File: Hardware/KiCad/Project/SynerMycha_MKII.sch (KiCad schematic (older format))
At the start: 1 part

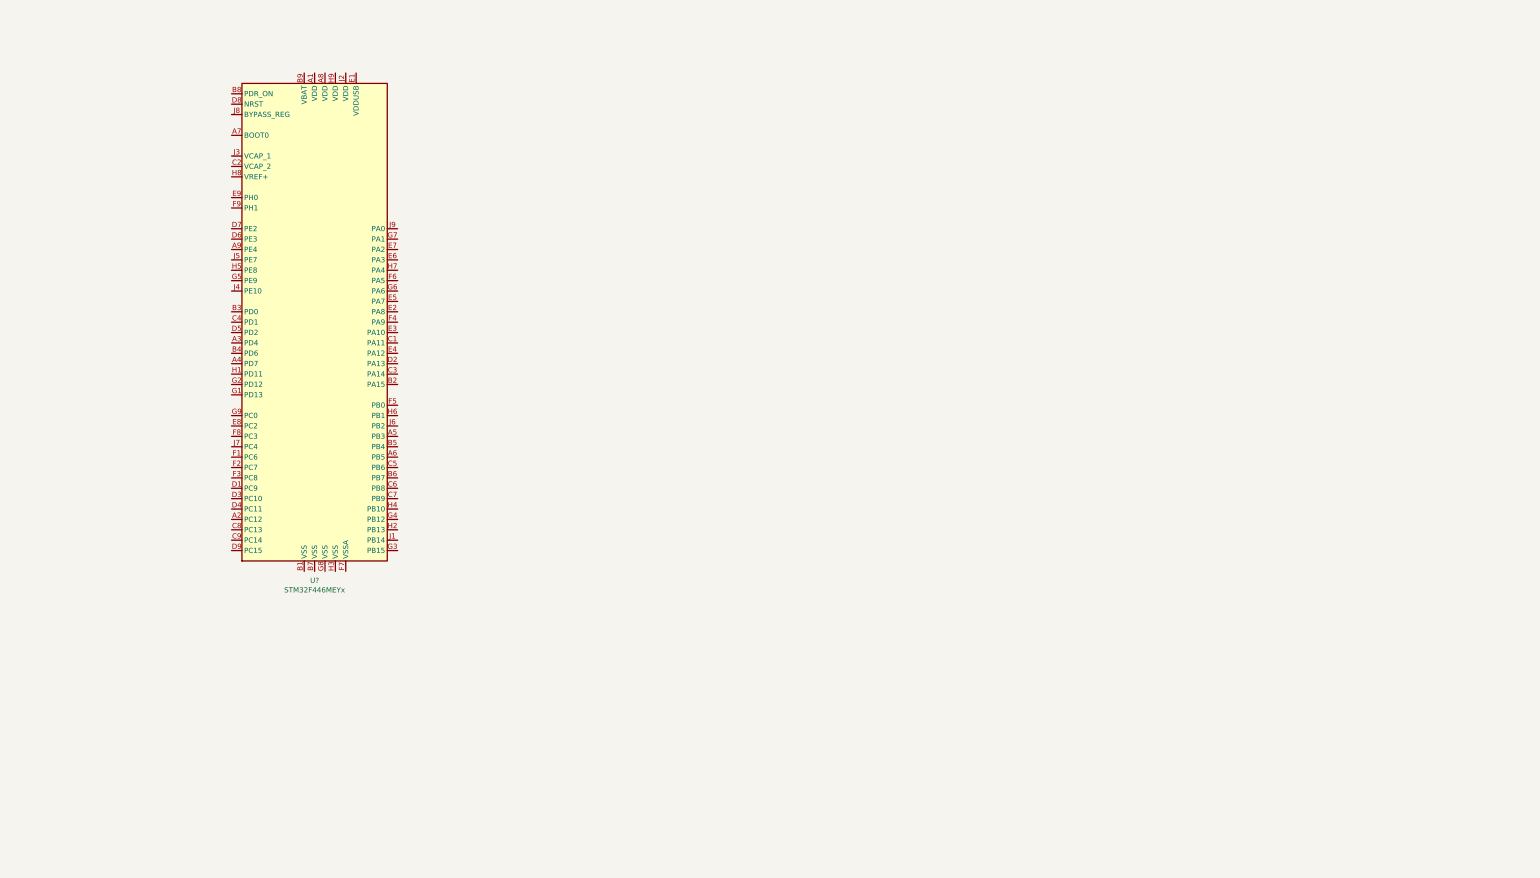
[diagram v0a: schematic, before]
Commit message: Basic uC config, added power and bluetooth antenna
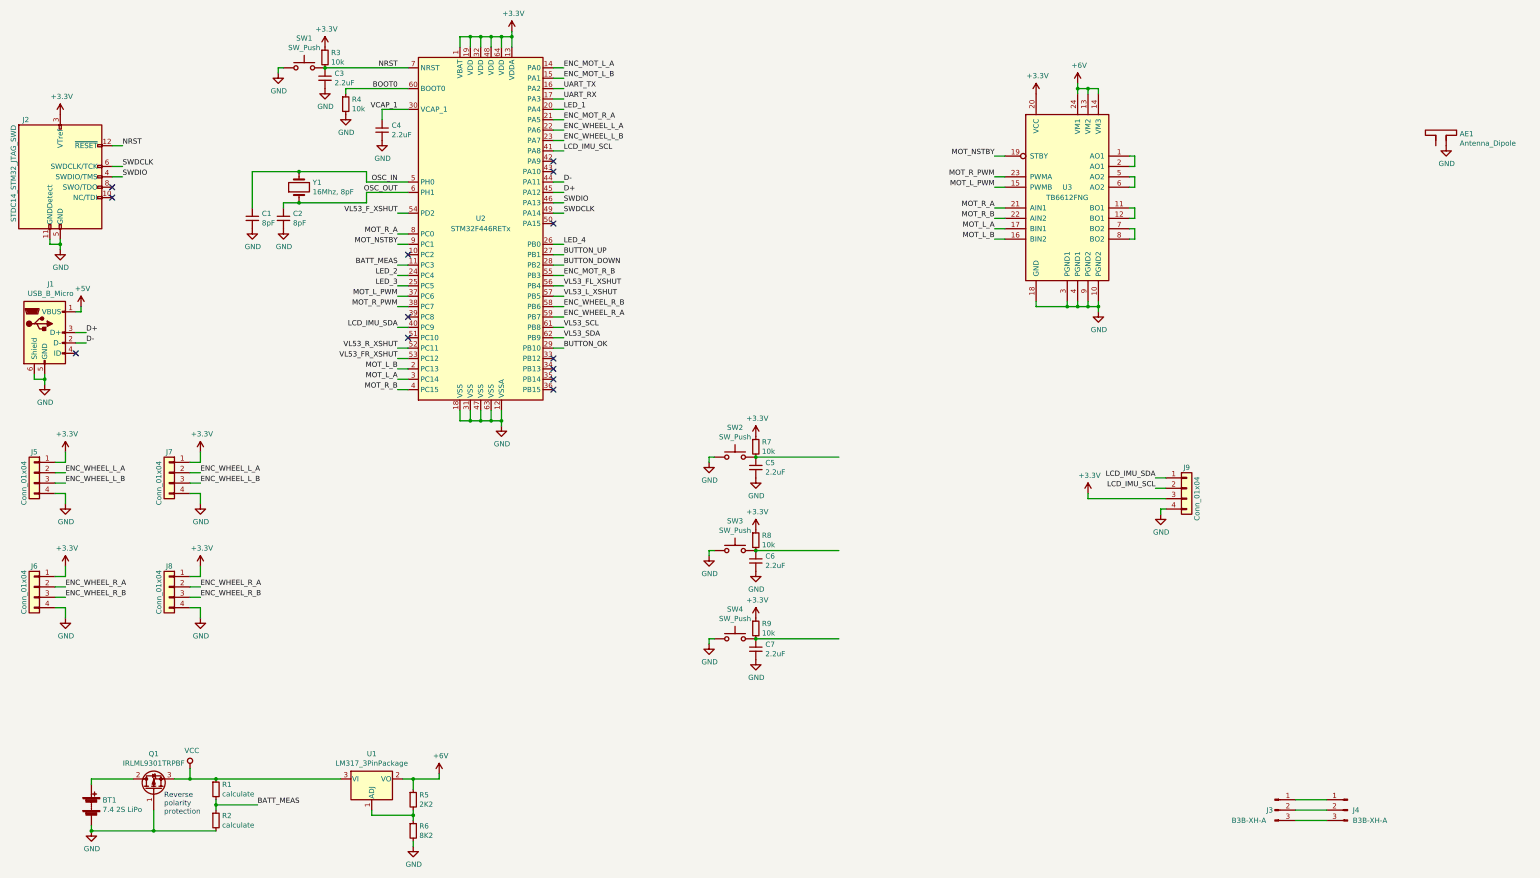
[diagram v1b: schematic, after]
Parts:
- removed U?: STM32F446MEYx, Package_CSP:ST_WLCSP-81_Die421, symbol MCU_ST_STM32F4:STM32F446MEYx
- added AE1: Antenna_Dipole, RF_Antenna:Texas_SWRA117D_2.4GHz_Right, symbol Device:Antenna_Dipole
- added BT1: 7.4 2S LiPo, symbol Device:Battery
- added C1, C2: 8pF, Capacitor_SMD:C_0402_1005Metric, symbol Device:C_Small
- added C3, C4, C5, C6, C7: 2.2uF, Capacitor_SMD:C_0603_1608Metric, symbol Device:C_Small
- added J1: USB_B_Micro, Connector_USB:USB_Micro-B_Amphenol_10103594-0001LF_Horizontal, symbol Connector:USB_B_Micro
- added J2: STDC14_STM32_JTAG_SWD, Connector_PinHeader_1.27mm:PinHeader_2x05_P1.27mm_Vertical_SMD, symbol STM32_STDC14:STDC14_STM32_JTAG_SWD
- added J3, J4: B3B-XH-A, Connector_JST:JST_XH_B3B-XH-A_1x03_P2.50mm_Vertical, symbol Connector:Conn_01x03_Male
- added J5, J6, J7, J8: Conn_01x04, Connector_PinHeader_1.00mm:PinHeader_1x04_P1.00mm_Vertical, symbol Connector_Generic:Conn_01x04
- added J9: Conn_01x04, Connector_PinHeader_2.54mm:PinHeader_1x04_P2.54mm_Vertical, symbol Connector_Generic:Conn_01x04
- added Q1: IRLML9301TRPBF, Package_TO_SOT_SMD:SOT-23, symbol Device:Q_PMOS_GDS
- added R1, R2: calculate, Resistor_SMD:R_0402_1005Metric, symbol Device:R_Small
- added R3, R4, R7, R8, R9: 10k, Resistor_SMD:R_0402_1005Metric, symbol Device:R_Small
- added R5: 2K2, Resistor_SMD:R_0402_1005Metric, symbol Device:R_Small
- added R6: 8K2, Resistor_SMD:R_0402_1005Metric, symbol Device:R_Small
- added SW1, SW2, SW3, SW4: SW_Push, Button_Switch_SMD:SW_SPST_B3U-1000P, symbol Switch:SW_Push
- added U1: LM317_3PinPackage, Package_TO_SOT_SMD:SOT-223, symbol Regulator_Linear:LM317_3PinPackage
- added U2: STM32F446RETx, Package_QFP:LQFP-64_10x10mm_P0.5mm, symbol MCU_ST_STM32F4:STM32F446RETx
- added U3: TB6612FNG, Package_SO:SSOP-24_5.3x8.2mm_P0.65mm, symbol Driver_Motor:TB6612FNG
- added Y1: 16Mhz, 8pF, Crystal:Crystal_SMD_TXC_7A-2Pin_5x3.2mm, symbol Device:Crystal
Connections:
- new net: BT1.1 (+), Q1.2 (D)
- new net: J3.1 (Pin_1), J4.1 (Pin_1)
- new net: J3.2 (Pin_2), J4.2 (Pin_2)
- new net: J3.3 (Pin_3), J4.3 (Pin_3)
- new net: C5.1, R7.2, SW2.2
- new net: C6.1, R8.2, SW3.2
- new net: C7.1, R9.2, SW4.2
- new net: U3.1 (AO1), U3.2 (AO1)
- new net: U3.11 (BO1), U3.12 (BO1)
- new net: U3.5 (AO2), U3.6 (AO2)
- new net: U3.7 (BO2), U3.8 (BO2)
- new net: R5.2, R6.1, U1.1 (ADJ)
- new net +3V3: J2.3 (VTref), J5.1 (Pin_1), J6.1 (Pin_1), J7.1 (Pin_1), J8.1 (Pin_1), J9.3 (Pin_3), R3.1, R7.1, R8.1, R9.1, U2.1 (VBAT), U2.13 (VDDA), U2.19 (VDD), U2.32 (VDD), U2.48 (VDD), U2.64 (VDD), U3.20 (VCC)
- new net +5V: J1.1 (VBUS)
- new net +6V: R5.1, U1.2 (VO), U3.13 (VM2), U3.14 (VM3), U3.24 (VM1)
- new net BATT_MEAS: R1.2, R2.1, U2.11 (PC3)
- new net BOOT0: R4.1, U2.60 (BOOT0)
- new net BUTTON_DOWN: U2.28 (PB2)
- new net BUTTON_OK: U2.29 (PB10)
- new net BUTTON_UP: U2.27 (PB1)
- new net D+: J1.3 (D+), U2.45 (PA12)
- new net D-: J1.2 (D-), U2.44 (PA11)
- new net ENC_MOT_L_A: U2.14 (PA0)
- new net ENC_MOT_L_B: U2.15 (PA1)
- new net ENC_MOT_R_A: U2.21 (PA5)
- new net ENC_MOT_R_B: U2.55 (PB3)
- new net ENC_WHEEL_L_A: J5.2 (Pin_2), J7.2 (Pin_2), U2.22 (PA6)
- new net ENC_WHEEL_L_B: J5.3 (Pin_3), J7.3 (Pin_3), U2.23 (PA7)
- new net ENC_WHEEL_R_A: J6.2 (Pin_2), J8.2 (Pin_2), U2.59 (PB7)
- new net ENC_WHEEL_R_B: J6.3 (Pin_3), J8.3 (Pin_3), U2.58 (PB6)
- new net GND: AE1.2, BT1.2 (-), C1.2, C2.2, C3.2, C4.2, C5.2, C6.2, C7.2, J1.5 (GND), J1.6 (Shield), J2.11 (GNDDetect), J2.5 (GND), J5.4 (Pin_4), J6.4 (Pin_4), J7.4 (Pin_4), J8.4 (Pin_4), J9.4 (Pin_4), Q1.1 (G), R2.2, R4.2, R6.2, SW1.1, SW2.1, SW3.1, SW4.1, U2.12 (VSSA), U2.18 (VSS), U2.31 (VSS), U2.47 (VSS), U2.63 (VSS), U3.10 (PGND2), U3.18 (GND), U3.3 (PGND1), U3.4 (PGND1), U3.9 (PGND2)
- new net LCD_IMU_SCL: J9.2 (Pin_2), U2.41 (PA8)
- new net LCD_IMU_SDA: J9.1 (Pin_1), U2.40 (PC9)
- new net LED_1: U2.20 (PA4)
- new net LED_2: U2.24 (PC4)
- new net LED_3: U2.25 (PC5)
- new net LED_4: U2.26 (PB0)
- new net MOT_L_A: U2.3 (PC14), U3.17 (BIN1)
- new net MOT_L_B: U2.2 (PC13), U3.16 (BIN2)
- new net MOT_L_PWM: U2.37 (PC6), U3.15 (PWMB)
- new net MOT_NSTBY: U2.9 (PC1), U3.19 (STBY)
- new net MOT_R_A: U2.8 (PC0), U3.21 (AIN1)
- new net MOT_R_B: U2.4 (PC15), U3.22 (AIN2)
- new net MOT_R_PWM: U2.38 (PC7), U3.23 (PWMA)
- new net NRST: C3.1, J2.12 (~RESET~), R3.2, SW1.2, U2.7 (NRST)
- new net OSC_IN: C1.1, U2.5 (PH0), Y1.2
- new net OSC_OUT: C2.1, U2.6 (PH1), Y1.1
- new net SWDCLK: J2.6 (SWDCLK/TCK), U2.49 (PA14)
- new net SWDIO: J2.4 (SWDIO/TMS), U2.46 (PA13)
- new net UART_RX: U2.17 (PA3)
- new net UART_TX: U2.16 (PA2)
- new net VCAP_1: C4.1, U2.30 (VCAP_1)
- new net VCC: Q1.3 (S), R1.1, U1.3 (VI)
- new net VL53_FL_XSHUT: U2.56 (PB4)
- new net VL53_FR_XSHUT: U2.53 (PC12)
- new net VL53_F_XSHUT: U2.54 (PD2)
- new net VL53_L_XSHUT: U2.57 (PB5)
- new net VL53_R_XSHUT: U2.52 (PC11)
- new net VL53_SCL: U2.61 (PB8)
- new net VL53_SDA: U2.62 (PB9)
- no-connect marks 0 -> 13
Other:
- note added: "Reverse \npolarity \nprotection"

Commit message: QS
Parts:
- removed AE1: Antenna_Dipole, RF_Antenna:Texas_SWRA117D_2.4GHz_Right, symbol Device:Antenna_Dipole
- removed U3: TB6612FNG, Package_SO:SSOP-24_5.3x8.2mm_P0.65mm, symbol Driver_Motor:TB6612FNG
- added BZ?: Buzzer, symbol Device:Buzzer
- added C10, C12, C13, C8: 0.1uF, Capacitor_SMD:C_0402_1005Metric, symbol Device:C_Small
- added C11, C14, C16, C9: 10uF, Capacitor_SMD:C_0603_1608Metric, symbol Device:C_Small
- added C15: 0.1uF, Capacitor_SMD:C_0603_1608Metric, symbol Device:C_Small
- added J10: USB_B_Micro, Connector_USB:USB_Micro-B_Amphenol_10103594-0001LF_Horizontal, symbol Connector:USB_B_Micro
- added J11: Conn_02x04_Odd_Even, Connector_PinSocket_2.54mm:PinSocket_2x04_P2.54mm_Horizontal, symbol Connector_Generic:Conn_02x04_Odd_Even
- added Q2, Q3: S8050, Package_TO_SOT_THT:TO-92_Inline, symbol Transistor_BJT:S8050
- added R10, R11: 10k, Resistor_SMD:R_0402_1005Metric, symbol Device:R_Small
- added R12, R13: 12k, Resistor_SMD:R_0402_1005Metric, symbol Device:R_Small
- added U3: VL53L0X, VL53L0X:SENSOR_VL53L0X, symbol VL53L0X:VL53L0X
- added U4: DRV8835, Package_SON:Texas_R-PWSON-N12_EP0.4x2mm, symbol KiCad_bibelem:DRV8835
- added U5, U6: AS5045B, Package_SO:SSOP-16_5.3x6.2mm_P0.65mm, symbol Sensor_Magnetic:AS5045B
- added U7: CP2102N-A01-GQFN28, Package_DFN_QFN:QFN-28-1EP_5x5mm_P0.5mm_EP3.35x3.35mm, symbol Interface_USB:CP2102N-A01-GQFN28
- J5, J6: footprint Connector_PinHeader_1.00mm:PinHeader_1x04_P1.00mm_Vertical -> Connector_PinHeader_1.00mm:PinHeader_1x04_P1.00mm_Horizontal
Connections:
- net labels added: ESP_D+, ESP_D-, ESP_VBUS, MOT_L_EN, MOT_L_PH, MOT_R_EN, MOT_R_PH, STM_D+, STM_D-
- net labels removed: D+, D-
- wire segments 191 -> 234
- no-connect marks 13 -> 44
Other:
- note added: "ENCODER BOARDS"
- note added: "MOTOR DRIVER"
- note added: "UI"
- note added: "WiFi"
- moved on the sheet: BT1, C1, C2, C5, C6, C7, J3, J4, J9, Q1, R1, R2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

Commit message: QS
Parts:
- removed J11: Conn_02x04_Odd_Even, Connector_PinSocket_2.54mm:PinSocket_2x04_P2.54mm_Horizontal, symbol Connector_Generic:Conn_02x04_Odd_Even
- removed Y1: 16Mhz, 8pF, Crystal:Crystal_SMD_TXC_7A-2Pin_5x3.2mm, symbol Device:Crystal
- added AE2: 2.4GHz, RF_Antenna:Texas_SWRA117D_2.4GHz_Right, symbol Device:Antenna_Loop
- added C17, C18: 10uF, Capacitor_SMD:C_0603_1608Metric, symbol Device:C_Small
- added C19: 1uF, Capacitor_SMD:C_0402_1005Metric, symbol Device:C_Small
- added C20, C21: 5.6pF, Capacitor_SMD:C_0402_1005Metric, symbol Device:C_Small
- added C22: 8.6pF, Capacitor_SMD:C_0402_1005Metric, symbol Device:C_Small
- added C23: 2.4pF, Capacitor_SMD:C_0402_1005Metric, symbol Device:C_Small
- added C24, C25, C26: 0.1uF, Capacitor_SMD:C_0603_1608Metric, symbol Device:C_Small
- added D1, D2, D3, D4, D5, D6, D7, D8: WS2812B, LED_SMD:LED_WS2812B_PLCC4_5.0x5.0mm_P3.2mm, symbol LED:WS2812B
- added D9: BLUE, LED_SMD:LED_0603_1608Metric, symbol Device:LED_Small
- added J12, J13, J14, J15, J16, J17: Conn_01x05, Connector_PinHeader_1.00mm:PinHeader_1x05_P1.00mm_Vertical_SMD_Pin1Left, symbol Connector_Generic:Conn_01x05
- added L1: 1.5nH, Inductor_SMD:L_0402_1005Metric, symbol Device:L_Small
- added R14, R15, R16: 10k, Resistor_SMD:R_0402_1005Metric, symbol Device:R_Small
- added R17, R19: 2K2, Resistor_SMD:R_0402_1005Metric, symbol Device:R_Small
- added R18, R20: 8K2, Resistor_SMD:R_0402_1005Metric, symbol Device:R_Small
- added R21, R22, R23, R24, R25, R26: 12K, Resistor_SMD:R_0402_1005Metric, symbol Device:R_Small
- added U10, U8: VL53L0X, VL53L0X:SENSOR_VL53L0X, symbol VL53L0X:VL53L0X
- added U11, U12: LM317_3PinPackage, Package_TO_SOT_SMD:SOT-223, symbol Regulator_Linear:LM317_3PinPackage
- added U4: ESP8266EX, Package_DFN_QFN:QFN-32-1EP_5x5mm_P0.5mm_EP3.45x3.45mm, symbol MCU_Espressif:ESP8266EX
- added U9: ESP-PSRAM32, Package_SO:SOIC-8_3.9x4.9mm_P1.27mm, symbol Memory_RAM:ESP-PSRAM32
- added Y1: 16Mhz, 8pF, Crystal:Crystal_SMD_Abracon_ABM10-4Pin_2.5x2.0mm, symbol Device:Crystal_GND24_Small
- added Y?: 26Mhz, 5.6pF, Crystal:Crystal_SMD_Abracon_ABM10-4Pin_2.5x2.0mm, symbol Device:Crystal_GND24_Small
- BZ1: renamed from BZ?; footprint (none) -> Buzzer_Beeper:Buzzer_CUI_CPT-9019S-SMT
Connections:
- net labels added: +2V8, +3V3, ESP_EN, ESP_GPIO0, ESP_GPIO2, ESP_RX, ESP_TX, ESP_~RESET
- net labels removed: +3.3V
- wire segments 234 -> 396
- no-connect marks 44 -> 36
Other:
- note added: "DISTANCE SENSOR BOARDS"
- note added: "RGB LEDS"
- note added: "RVP, VOLTAGE SOURCES"
- moved on the sheet: BT1, C13, C14, C15, C16, J10, J3, J4, Q1, Q2, Q3, R1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
